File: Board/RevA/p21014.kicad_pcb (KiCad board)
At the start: 2 copper layers, 53.3 x 25.4 mm, 23 parts, among them J1 Conn_01x06_Male, J2 Conn_01x06_Male, J3 Conn_02x03, J4 Conn_01x08_Female, J5 Conn_01x12_Female, J6 Conn_01x06_Female, SW1 SW_Push

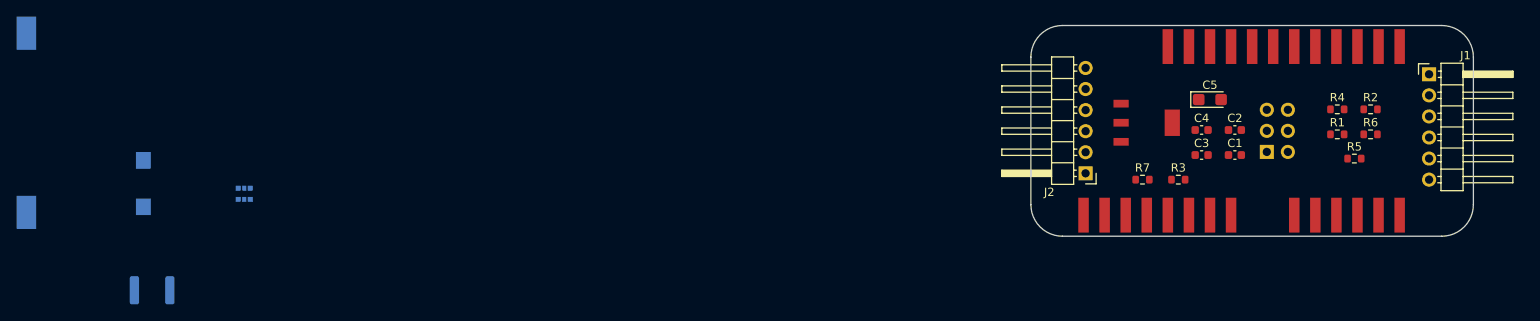
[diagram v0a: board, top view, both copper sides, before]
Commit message: Added All Proper Footprints to Layout
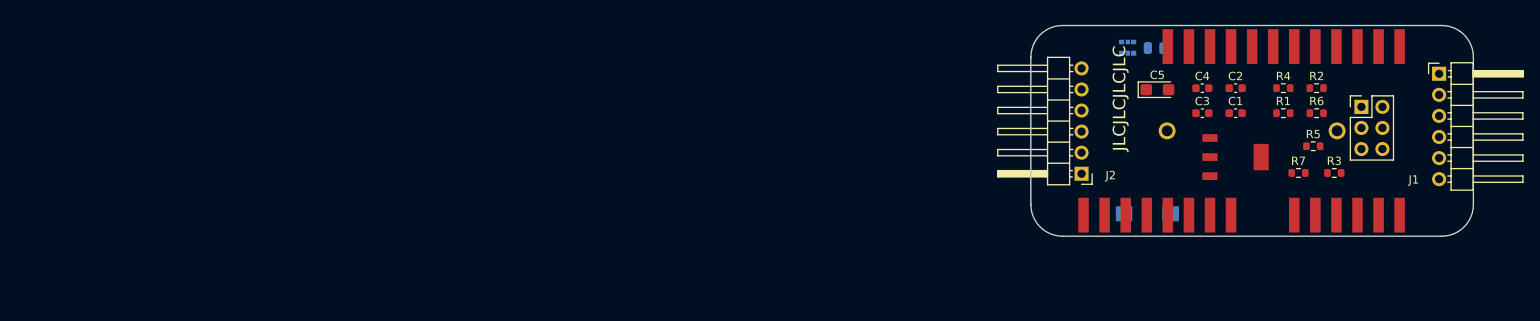
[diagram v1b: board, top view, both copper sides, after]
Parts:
- BT1: footprint 0_MSD_FPs:AJS-Coin-Cell_1062-Digikey -> 0_MSD_FPs:AJS-Coin-Cell_1027-Digikey
- D2: footprint LED_SMD:LED_1812_4532Metric -> 0_MSD_FPs:LED_0805_2012Metric
- J3: moved to F.Cu
- moved BT1 137.9 mm to (189.9, 60.2)
- moved D2 124.4 mm to (188.5, 50.2), turned to 180 degrees
- moved SW1 118.2 mm to (184.7, 70.2), turned to 270 degrees
- moved D1 107.9 mm to (184.4, 50.8)
- moved R7 18.8 mm to (205.7, 65.2)
- moved R3 18.8 mm to (210.1, 65.2)
- moved J3 12.6 mm to (213.3, 57.3)
- moved VR1 11.5 mm to (198.2, 63.3)
- moved R2 6.99 mm to (207.9, 55.0)
- moved R6 6.99 mm to (207.9, 58.0)
- moved R1 6.99 mm to (203.9, 58.0)
- moved R4 6.99 mm to (203.9, 55.0)
- moved C5 6.44 mm to (188.7, 55.2)
- moved R5 5.18 mm to (207.5, 62.0)
- moved C1 5.04 mm to (198.2, 58.0)
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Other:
- board text added: "JLCJLCJLCJLC"

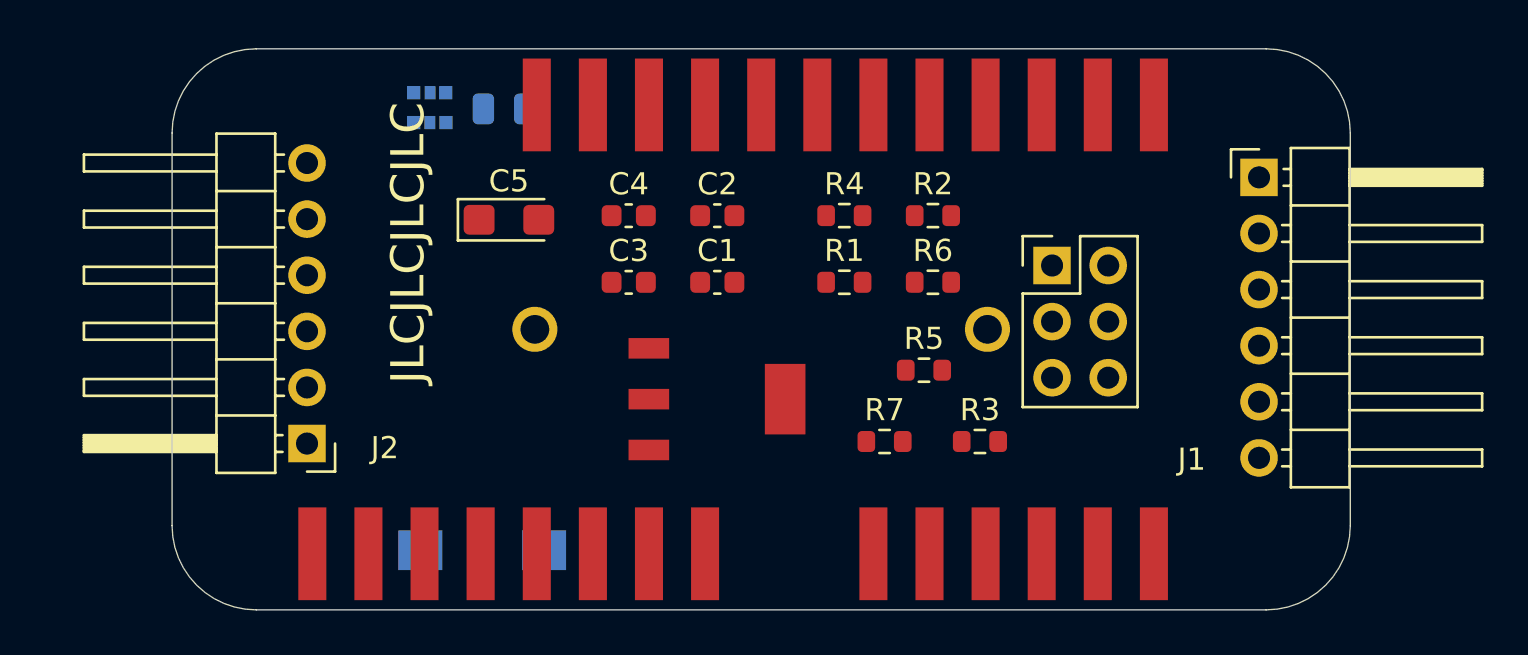
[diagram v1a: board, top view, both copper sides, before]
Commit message: Finished Layout RevA Board
Still needs routing.
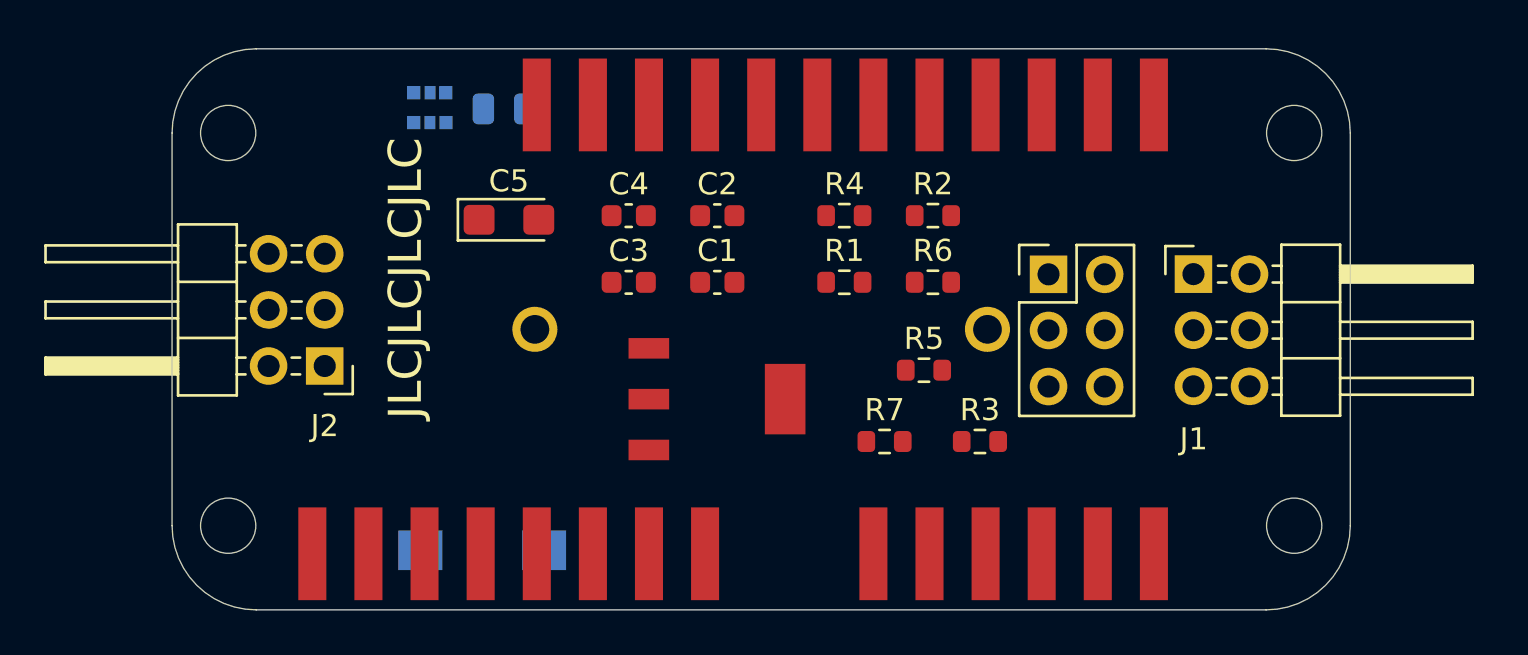
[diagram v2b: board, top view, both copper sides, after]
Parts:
- added MH1: MountingHole_2.5mm, MountingHole:MountingHole_2.5mm, F.Cu at (176.0, 51.3)
- added MH2: MountingHole_2.5mm, MountingHole:MountingHole_2.5mm, F.Cu at (224.3, 51.3)
- added MH3: MountingHole_2.5mm, MountingHole:MountingHole_2.5mm, F.Cu at (224.3, 69.0)
- added MH4: MountingHole_2.5mm, MountingHole:MountingHole_2.5mm, F.Cu at (176.0, 69.0)
- J1, J2: footprint Connector_PinHeader_2.54mm:PinHeader_1x06_P2.54mm_Horizontal -> Connector_PinHeader_2.54mm:PinHeader_2x03_P2.54mm_Horizontal
- moved J1 5.29 mm to (219.7, 57.7)
- moved J2 3.60 mm to (180.4, 61.8)
- moved J3 0.43 mm to (213.2, 57.7)

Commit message: Completely Finished RevA Board
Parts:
- added G55: LOGO, 0_MSD_FPs:RIT_Logo, B.Cu at (184.4, 60.3)
- moved J2 0.90 mm to (180.6, 62.7)
- moved J3 0.05 mm to (213.2, 57.6)
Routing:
- net GNDREF: track 0.00 -> 109.2 mm, vias 0 -> 1
- net /SDA: track 0.00 -> 81.0 mm
- net /SCL: track 0.00 -> 77.3 mm
- net +5V: track 0.00 -> 70.2 mm
- net Net-(D1-Pad2): track 0.00 -> 60.3 mm, vias 0 -> 1
- net /RST: track 0.00 -> 58.6 mm, vias 0 -> 2
- net Net-(J3-Pad5): track 0.00 -> 53.1 mm, vias 0 -> 1
- net Net-(J3-Pad4): track 0.00 -> 36.5 mm
- net Net-(J3-Pad2): track 0.00 -> 30.8 mm, vias 0 -> 1
- net Net-(D1-Pad1): track 0.00 -> 28.4 mm, vias 0 -> 1
- net Net-(D1-Pad3): track 0.00 -> 25.9 mm, vias 0 -> 1
- net +BATT: track 0.00 -> 25.4 mm, vias 0 -> 2
- net Net-(D2-Pad2): track 0.00 -> 20.0 mm, vias 0 -> 1
- net /Feather_Board/BLUE: track 0.00 -> 16.8 mm, vias 0 -> 2
- net Net-(J3-Pad3): track 0.00 -> 16.1 mm
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- added copper zone on B.Cu, net GNDREF
- added copper zone on F.Cu, net GNDREF
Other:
- board text added: "2*CR2330 Batteries"
- board text added: "P21014 MSD 2021"
- board text added: "RevA"

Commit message: Updated RevA Parts List/Digikey Order 1
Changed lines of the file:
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@@
       (outputformat 1)
       (mirror false)
-      (drillshape 1)
+      (drillshape 0)
       (scaleselection 1)
-      (outputdirectory ""))
+      (outputdirectory "../##Gerber/RevA/"))
   )
   (net 0 "")
@@
       (effects (font (size 0.8 0.8) (thickness 0.12)))
     )
-    (pad 1 smd roundrect (at -1.35 0) (size 1.4 1.35) (layers F.Cu F.Paste F.Mask) (roundrect_rratio 0.185185)
+    (pad 1 smd roundrect (at -1.35 0) (size 1.4 1.35) (layers F.Cu F.Paste F.Mask) (roundrect_rratio 0.1851844444444445)
       (net 4 +5V))
-    (pad 2 smd roundrect (at 1.35 0) (size 1.4 1.35) (layers F.Cu F.Paste F.Mask) (roundrect_rratio 0.185185)
+    (pad 2 smd roundrect (at 1.35 0) (size 1.4 1.35) (layers F.Cu F.Paste F.Mask) (roundrect_rratio 0.1851844444444445)
       (net 1 GNDREF))
     (model ${KISYS3DMOD}/Capacitor_Tantalum_SMD.3dshapes/CP_EIA-3216-18_Kemet-A.wrl
